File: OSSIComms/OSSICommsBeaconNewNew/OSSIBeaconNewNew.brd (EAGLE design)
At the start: 94 x 88 mm, 77 parts, among them Q1 NX-3215, U1 OPA2347, U2 MSP430F2132, U3 LM7321, U4 MAX1682, U5 MAX890L, U6 MAX4376, U7 TPS3838, U8 MCP1700_SOT23, X1 ESQ-126-38-G-D, X2 5268-03, X3 ICCON_POWERCON, X4 ICCON_POWERCON, X5 WEIDMULLER, X6 JTAG10PINMINI-H, X7 5268-03

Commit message: beacon newnew led new
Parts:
- removed JP2: (no value), OSSI:JP1
- removed LED3: (no value), SparkFun:LED-0603
- removed Q1: NX-3215, OSSI:NX-3215
- removed R33: 1k, OSSI:R0603(1608)
- removed R63, R67: 250, OSSI:R0603(1608)
- removed R71: 10k, OSSI:R0603(1608)
- removed TP1, TP2, TP3, TP4, TP5, TP6, TP7: TP, OSSI:TP-13
- removed TR2: FDV301N, OSSI:SOT23
- removed X6: JTAG10PINMINI-H, OSSI:M50-3200545
- removed X7: 5268-03, OSSI:5268-03
- added C13: 22nF, OSSI:C0603(1608)
- added C14: 1uF,0603, OSSI:C0603(1608)
- added C15: 100pF, OSSI:C0603(1608)
- added C16: 1uF 0805, OSSI:C0805(2012)
- added C19, C33: 1uF, OSSI:C0603(1608)
- added C20: (no value), OSSI:C0603(1608)
- added C21, C25: 1nF, OSSI:C0603(1608)
- added C22, C23, C24: 22pF, OSSI:C0603(1608)
- added C26, C31: 10nF, OSSI:C0603(1608)
- added C27: DNP, OSSI:C0603(1608)
- added C28: 22uF,1210, OSSI:C1210-GCM32
- added C29, C30: 10uF, LDO Tantal 16V, OSSI:C1206(3216)-A
- added C32, C34, C35, C36, C40, C42: 100nF, OSSI:C0603(1608)
- added C37, C41: TBD, OSSI:C0603(1608)
- added C38, C39: 12.5pF, OSSI:C0603(1608)
- added D1: BAT54S, OSSI:SOT23
- added F1: LFCN-160, OSSI:LFCN
- added L1, L3: 470nH, 1008 size, OSSI:L1008(2520)
- added L2: 10nH, OSSI:L0603(1608)
- added L4, L5: 68nH, OSSI:L0603(1608)
- added L6: 5~15R ferrite bead, OSSI:L0805(2012)
- added Q2: NX-3215, OSSI:NX-3215
- added R26: 4.7k, OSSI:R0603(1608)
- added R27: 47k, OSSI:R0603(1608)
- added R28: 1M, OSSI:R0603(1608)
- added TCXO1: 19.2MHz, OSSI:TCXO_M532
- added U10: NC7SZ04, OSSI:SC70-5
- added U9: MAX6369, OSSI:SOT23-8
- C1: value 1uF -> 100nF
- C10: value 100nF -> 1000pF
- C11: value 10uF, LDO Tantal 16V -> 22pF; device OSSI:C1206(3216)-A -> OSSI:C0603(1608)
- C12: value 10uF, LDO Tantal 16V -> 68pF; device OSSI:C1206(3216)-A -> OSSI:C0603(1608)
- C17: value 12.5pF -> 2.2uF, 0805; device OSSI:C0603(1608) -> OSSI:C0805(2012)
- C18: value 12.5pF -> 100pF
- C2: value 100nF -> 1uF
- C3: value 100nF -> 22uF,1210; device OSSI:C0603(1608) -> OSSI:C1210-GCM32
- C4: value 100nF -> 1uF,0805; device OSSI:C0603(1608) -> OSSI:C0805(2012)
- C6: value 10uF, LDO Tantal 16V -> 10nF; device OSSI:C1206(3216)-A -> OSSI:C0603(1608)
- C7: value 100nF -> 10nF
- C8: value 1uF 0805 -> 10nF; device OSSI:C0805(2012) -> OSSI:C0603(1608)
- C9: value 1206 Cap -> (none); device OSSI:C1206-GCM31 -> OSSI:C0603(1608)
- LED1: device led:CHIPLED_0603 -> SparkFun:LED-0603
- R1, R10: value TBD -> 100k
- R11: value 4.7k -> 23.7k
- R12, R8: value 4.7k -> 0
- R13: value 10k -> 4.7k
- R14: value 47k -> 4.7k
- R15, R17, R21: value (none) -> 100k
- R18: value 1k -> 4.7k
- R19: value (none) -> 4.7k
- R20: value (none) -> 10k
- R22: value 0.005, 2W RSENSE -> 250; device OSSI:R4527(12070) -> OSSI:R0603(1608)
- R23: value 0 -> 1k
- R24: value 1.1k -> 10k
- R25: value 2.2k -> 250
- R3: value 100k -> 6.2k
- R4: value 1k -> 100k
- R5: value 100k -> 5.1k
- R6: value 100k -> 2.4k
- R7: value 1.5k -> 3.6k
- R9: value DNP -> 100k
- TR1: value FDD8896 -> FDV301N; device OSSI:TO252 -> OSSI:SOT23
- U1: value OPA2347 -> MAX890L; device OSSI:SOT23-8DCN -> OSSI:SO8
- U2: value MSP430F2132 -> ADL5530; device OSSI:PW28 -> OSSI:LFCSP8_CP
- U3: value LM7321 -> ADF7012; device OSSI:SO8 -> OSSI:TSSOP24
- U4: value MAX1682 -> MCP1700_SOT23; device OSSI:SOT23-5DBV -> OSSI:SOT23
- U6: value MAX4376 -> TPS3838
- U7: value TPS3838 -> OPA2347; device OSSI:SOT23-5DBV -> OSSI:SOT23-8DCN
- U8: value MCP1700_SOT23 -> MSP430F2132; device OSSI:SOT23 -> OSSI:PW28
- X2: value 5268-03 -> RFCON-MCX-R/A; device OSSI:5268-03 -> OSSI:MCX-R/A
- X3: value ICCON_POWERCON -> JTAG10PINMINI-H; device OSSI:ICCON6643220-1 -> OSSI:M50-3200545
- X4: value ICCON_POWERCON -> 5268-03; device OSSI:ICCON6643220-1 -> OSSI:5268-03
- X5: value WEIDMULLER -> 5268-02; device OSSI:WEIDMULLER1760490000 -> OSSI:5628-02
- moved R4 69.1 mm to (72.4, 71.1), turned to 0 degrees
- moved U1 67.1 mm to (73.7, 59.7)
- moved C2 66.2 mm to (71.1, 64.8), turned to 180 degrees
- moved U$1 61.4 mm to (76.2, 85.1)
- moved R18 56.4 mm to (43.2, 74.3), turned to 270 degrees
- moved R2 56.4 mm to (73.7, 64.8), turned to 0 degrees
- moved X2 55.8 mm to (8.89, 19.1), turned to 90 degrees
- moved C3 54.2 mm to (25.4, 9.53)
- moved R21 51.3 mm to (8.89, 64.8), turned to 180 degrees
- moved R10 49.5 mm to (63.5, 69.8), turned to 0 degrees
- moved C9 45.7 mm to (15.2, 19.1), turned to 180 degrees
- moved C6 44.3 mm to (26.0, 15.2), turned to 180 degrees
- moved C17 43.9 mm to (56.5, 12.1), turned to 90 degrees
- moved R16 43.6 mm to (16.5, 64.8), turned to 180 degrees
- moved R19 43.2 mm to (45.7, 74.3), turned to 270 degrees
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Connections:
- removed net 3.3VLED: C10.1, C11.1, C2.1, C7.1, R10.1, R13.2, R2.2, R71.2, U1.8, U2.2, U6.3, U7.5, U8.2, X2.1, X6.4
- removed net ACLK_OUT: TP2.TP, U2.8
- removed net ADC2: U1.6, U1.7, U2.10
- removed net PWM: JP2.1, R19.2, R20.1
- removed net RESET_LED: R2.1, R8.2, U2.7, U7.4
- removed net SMCLK_OUT: TP1.TP, U2.25, X6.7
- removed net STRUT_GND: H1.B3,2
- removed net SUN: R18.2, X2.2
- new net 3.3VBEACON: C28.P$1, C30.1, C31.1, C35.1, C36.1, D1.2, L6.1, R1.2, R20.2, R24.2, R9.2, U4.2, U6.5, U7.8, U8.2, U9.4, U9.5, U9.6, U9.8, X3.4, X5.1
- new net ADC0: U7.6, U7.7, U8.8
- new net BEACON_CE: U3.14, U8.18
- new net BEACON_CWCONTROL: R26.2, R27.1, X5.2
- new net BEACON_DATA: U3.4, U8.24
- new net BEACON_MUXOUT: U3.6, U8.22
- new net BEACON_RFOUT: C24.2, C7.1, L5.2
- new net BEACON_SCLK: U3.11, U8.21
- new net BEACON_SDATA: U3.12, U8.20
- new net BEACON_SLE: U3.13, U8.19
- new net BEACON_TXCLK: U3.5, U8.23
- new net BEACON_WDT_RST: C40.1, U6.3, U9.7
- new net N$1: R23.1, U8.11
- new net N$2: U8.27, X3.3
- new net N$34: C8.2, F1.1
- new net N$35: C9.1, F1.3
- new net N$36: C23.2, L4.2, L5.1
- new net N$37: C9.2, X2.1
- new net N$38: C25.2, C27.1, R28.2, U10.2
- new net N$40: C30.2, R12.1
- new net N$666: C29.1, C34.1, U4.3, U5.6, U5.7
- new net N$69: C25.1, TCXO1.3
- new net OSC1: C27.2, U3.8
- new net OSC2: R28.1, U10.4, U3.9
- new net PA_-FAULT: R1.1, U1.8, U8.3
- new net PA_ON: R4.2, TR1.1, U8.17
- new net RESETBEACON: R14.2, R9.1, U6.4, U8.7
- new net VBEACON_PA: C1.1, C3.P$1, C4.1, C5.1, C6.1, L1.P$1, U1.6, U1.7
- new net VCCRF: C14.1, C15.1, C20.1, C26.1, C32.1, L6.2, R8.1, TCXO1.4, U10.5, U3.1
- net ADC1: now also U7.1, U7.2, U8.9; no longer U1.1, U1.2, U2.9
- net BEACON_-FAULT: now also U5.8
- net BEACON_OFF: now also C33.1, R10.2, U5.3
- net BEACON_SCL: now also R24.1, R25.1
- net BEACON_SDA: now also R20.1, R22.1
- net BUS_CS: now also R15.1
- net GND: now also C11.2, C12.1, C14.2, C15.2, C16.1, C17.1, C19.2, C20.2, C22.1, C23.1, C24.1, C26.2, C28.P$2, C29.2, C3.P$2, C31.2, C32.2, C33.2, C34.2, C35.2, C36.2, C37.2, C38.2, C39.2, C40.2, C41.2, C42.2, C6.2, D1.1, F1.2, F1.4, R10.1, R11.1, R12.2, R13.2, R16.2, R27.2, R4.1, R7.1, TCXO1.1, TCXO1.2, TR1.2, U10.3, U2.1, U2.3, U2.5, U2.6, U2.8, U3.19, U3.22, U3.7, U6.1, U7.4, U8.4, U9.2, X2.2, X2.4, X2.5, X3.9; no longer C10.2, C12.2, C17.2, C3.2, C7.2, C8.2, C9.P$2, LED3.C, R1.1, R14.1, R17.2, R20.2, R23.2, R24.2, R25.1, R9.2, TP3.TP, TR2.2, U3.4, U7.1, U7.2, U8.1, X4.10, X4.2, X4.3, X4.4, X4.5, X4.6, X4.7, X4.8, X4.9, X5.2, X6.9, X7.1
- net LED_-FAULT: no longer U5.8
- net LED_OFF: no longer C1.1, R3.2, U5.3
- net LED_SCL: no longer R67.1, R71.1
- net LED_SDA: no longer R13.1, R63.1
- net N$10: now also R25.2, U8.13; no longer R1.2, U5.5
- net N$11: now also R18.2, U8.16; no longer R4.2, R5.2, R6.1
- net N$12: now also U8.10, U9.1; no longer R22.P$2, R7.1, TP6.TP, U6.5, X3.1, X3.10, X3.2, X3.3, X3.4, X3.5, X3.6, X3.7, X3.8, X3.9
- net N$13: now also C42.1, D1.3, R26.1, U8.14; no longer C9.P$1, U3.7, U4.2
- net N$14: now also L2.1, U3.16; no longer R16.1, R25.2, U3.6
- net N$15: now also L2.2, U3.15; no longer U2.27, X6.3
- net N$16: now also C13.1, C16.2, U3.24; no longer R22.P$1, TP7.TP, TR1.S, U6.4
- net N$17: now also C13.2, U3.17; no longer C11.2, R23.1
- net N$18: now also R7.2, U3.23; no longer R24.1, U3.2
- net N$19: now also C2.1, R2.1, TR1.3, U1.3; no longer C17.1, Q1.2, U2.5
- net N$20: now also C10.1, R6.1; no longer C18.1, Q1.1, U2.6
- net N$21: now also R3.2, U1.5; no longer JP1.2, LED3.A, R33.2
- net N$22: now also C41.1, R17.2, R21.1, U7.5; no longer R63.2, U2.12
- net N$23: now also C21.2, L3.P$2, U3.20; no longer R67.2, U2.13
- net N$24: now also C11.1, R5.1, U3.18; no longer R15.1, U6.1
- net N$25: now also C17.2, U3.2; no longer R33.1, U2.14
- net N$26: now also C10.2, C12.2, R5.2, U3.3; no longer C6.2, U4.3
- net N$27: now also C18.1, C19.1, L3.P$1, R8.2, U3.21; no longer C6.1, U4.5
- net N$28: now also C7.2, U2.2; no longer R12.2, U2.16
- net N$29: now also C21.1, C22.2, L4.1; no longer LED1.A, R7.2
- net N$3: now also U8.26, X3.5; no longer U2.28, X6.1
- net N$30: now also C8.1, L1.P$2, U2.7; no longer R15.2, R17.1, TR2.1
- net N$31: now also R14.1, X3.10; no longer U2.26, X6.5
- net N$32: now also R11.2, U5.5; no longer R8.1, X6.10
- net N$33: now also C37.1, R15.2, R16.1, U7.3; no longer JP2.2, U2.18
- net N$39: now also R19.2, U8.15; no longer R11.2, U2.15
- net N$4: now also U8.25, X3.7; no longer R10.2, U2.3
- net N$5: now also C38.1, Q2.2, U8.5; no longer C12.1, C3.1, U5.6, U5.7, U8.3
- net N$6: now also C39.1, Q2.1, U8.6; no longer R16.2, R9.1, TP5.TP, TR1.G, TR2.3
- net N$7: now also JP1.2, LED1.A, R23.2; no longer C4.1, R4.1, U1.3
- net N$8: now also U8.28, X3.1; no longer C5.1, R18.1, U1.5
- net N$9: now also R22.2, U8.12; no longer R19.1, R21.1, U3.3
- net RXD: now also R18.1, X4.3; no longer R12.1, X7.3
- net TEST: now also R13.1, U8.1, X3.8; no longer R14.2, U2.1, X6.8
- net TXD: now also R19.1, X4.2; no longer R11.1, X7.2
- net VBUS: now also R17.1, R2.2, U1.1, U1.2
- net VSUPERCAP: now also X1.13; no longer C8.1, R5.1, TP4.TP, TR1.D, U4.4, X5.1
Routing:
- net 3.3VLED: track 226.5 -> 0.00 mm, vias 2 -> 0
- net VSUPERCAP: track 89.2 -> 0.00 mm, vias 23 -> 0
- net LED_SCL: track 85.9 -> 0.00 mm, vias 2 -> 0
- net LED_SDA: track 82.0 -> 0.00 mm, vias 2 -> 0
- net BEACON_DATA: track 0.00 -> 65.5 mm
- net BEACON_TXCLK: track 0.00 -> 63.3 mm
- net BEACON_MUXOUT: track 0.00 -> 61.1 mm
- net SUN: track 52.8 -> 0.00 mm
- net BEACON_SLE: track 0.00 -> 49.5 mm
- net BEACON_CE: track 0.00 -> 49.4 mm
- net N$3: track 46.7 -> 0.00 mm, vias 2 -> 0
- net RESET_LED: track 46.2 -> 0.00 mm, vias 2 -> 0
- net SMCLK_OUT: track 45.4 -> 0.00 mm, vias 2 -> 0
- net N$31: track 43.4 -> 0.00 mm, vias 2 -> 0
- net N$15: track 45.0 -> 4.12 mm, vias 2 -> 0
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- removed copper zone on layer 1, net GND
- removed copper zone on layer 16, net GND
- removed copper zone on layer 16, net N$1
- removed copper zone on layer 1, net N$12
- removed copper zone on layer 1, net N$16
- removed copper zone on layer 16, net N$2
- removed copper zone on layer 16, net N$56
- removed copper zone on layer 1, net N$6
- removed copper zone on layer 1, net STRUT_GND
- removed copper zone on layer 1, net VBUS
- removed copper zone on layer 1, net VSOLAR
- removed copper zone on layer 1, net VSUPERCAP
- removed copper zone on layer 16, net VSUPERCAP
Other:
- board size 94 x 88 mm -> 92 x 92 mm
- board text removed: "ACLK"
- board text removed: "GND"
- board text removed: "LED+"
- board text removed: "PWM"
- board text removed: "RXD"
- board text removed: "SMCLK"
- board text removed: "SUN"
- board text removed: "TXD"
- board text removed: "VLED"
- board text removed: "VSUPERCAP"

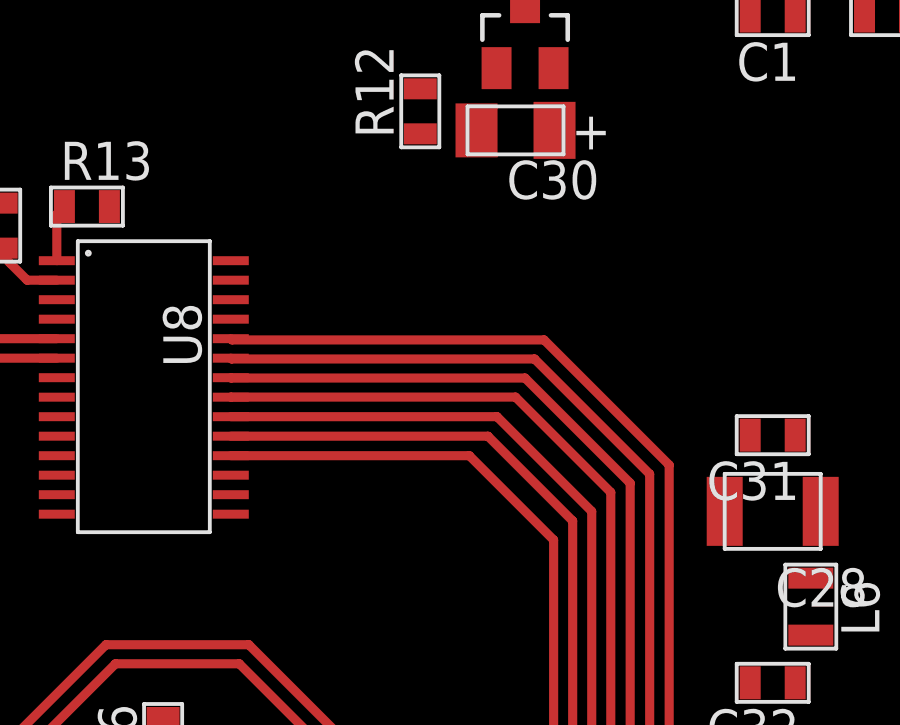
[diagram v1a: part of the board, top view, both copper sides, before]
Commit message: series resistor added
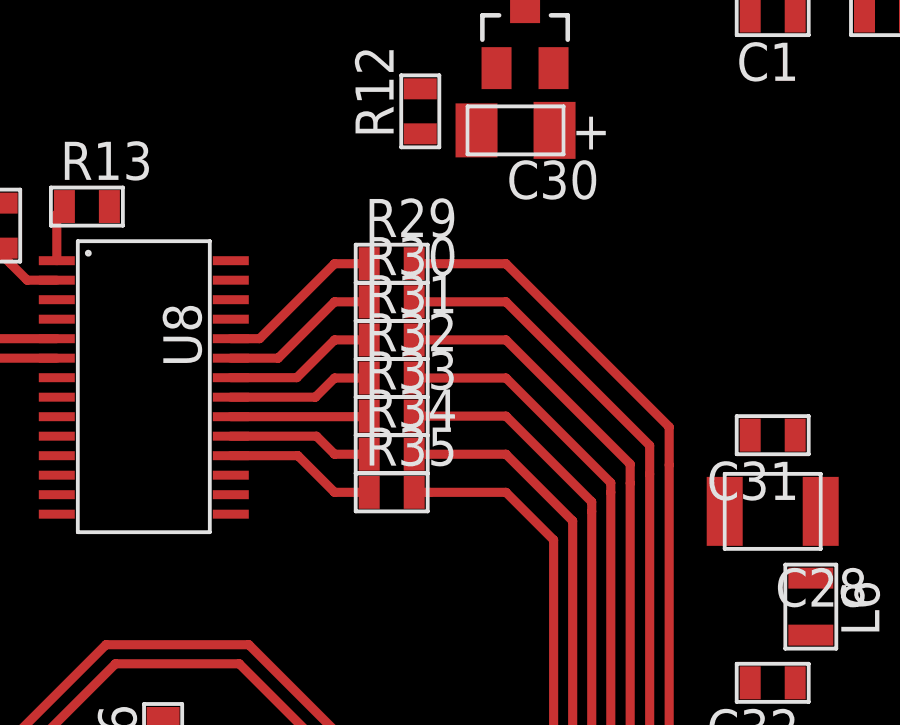
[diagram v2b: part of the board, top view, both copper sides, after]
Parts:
- added R29, R30, R31, R32, R33, R34, R35: 4.7k, OSSI:R0603(1608)
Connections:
- new net N$41: R29.1, U8.24
- new net N$42: R30.1, U8.23
- new net N$43: R31.1, U8.22
- new net N$44: R32.1, U8.21
- new net N$45: R33.1, U8.20
- new net N$46: R34.1, U8.19
- new net N$47: R35.1, U8.18
- net BEACON_CE: now also R35.2; no longer U8.18
- net BEACON_DATA: now also R29.2; no longer U8.24
- net BEACON_MUXOUT: now also R31.2; no longer U8.22
- net BEACON_SCLK: now also R32.2; no longer U8.21
- net BEACON_SDATA: now also R33.2; no longer U8.20
- net BEACON_SLE: now also R34.2; no longer U8.19
- net BEACON_TXCLK: now also R30.2; no longer U8.23
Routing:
- net BEACON_CE: track 49.4 -> 42.8 mm
- net BEACON_SLE: track 49.5 -> 43.2 mm
- net BEACON_SDATA: track 37.0 -> 31.1 mm
- net BEACON_SCLK: track 39.8 -> 34.1 mm
- net N$41: track 0.00 -> 5.65 mm
- net N$42: track 0.00 -> 5.39 mm
- net BEACON_MUXOUT: track 61.1 -> 55.9 mm
- net N$43: track 0.00 -> 5.13 mm
- net N$47: track 0.00 -> 5.12 mm
- net N$44: track 0.00 -> 4.88 mm
- net N$46: track 0.00 -> 4.86 mm
- net BEACON_TXCLK: track 63.3 -> 58.5 mm
- net N$45: track 0.00 -> 4.62 mm
- net BEACON_DATA: track 65.5 -> 61.1 mm

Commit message: beacon almost done
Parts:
- moved R4 35.6 mm to (56.2, 39.4), turned to 90 degrees
- moved TR1 32.2 mm to (58.7, 39.4), turned to 270 degrees
- moved C37 29.3 mm to (22.9, 37.5)
- moved R1 28.0 mm to (48.3, 55.2), turned to 180 degrees
- moved R15 26.8 mm to (25.4, 38.7)
- moved R16 26.8 mm to (22.9, 38.7)
- moved C41 23.1 mm to (22.9, 47.6)
- moved R17 23.1 mm to (25.4, 46.4)
- moved R21 23.1 mm to (22.9, 46.4)
- moved U7 20.4 mm to (22.9, 42.5), turned to 0 degrees
- moved C35 17.1 mm to (20.3, 42.5), turned to 270 degrees
- moved R23 12.6 mm to (30.8, 54.9), turned to 90 degrees
- moved C40 10.6 mm to (29.5, 48.3), turned to 90 degrees
- moved R2 10.2 mm to (73.7, 74.9)
- moved C1 9.52 mm to (72.4, 63.5)
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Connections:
- new net STRUT_GND: H1.B3,2
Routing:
- net 3.3VBEACON: track 2.42 -> 200.3 mm, vias 0 -> 8
- net VBUS: track 0.00 -> 122.6 mm, vias 0 -> 1
- net VBEACON_PA: track 7.44 -> 120.3 mm
- net N$2: track 0.00 -> 100.0 mm, vias 0 -> 1
- net VCCRF: track 19.0 -> 87.1 mm, vias 0 -> 4
- net BUS_CS: track 0.00 -> 67.8 mm, vias 0 -> 1
- net RESETBEACON: track 0.00 -> 63.2 mm, vias 0 -> 4
- net N$19: track 0.00 -> 53.7 mm, vias 0 -> 4
- net GND: track 4.46 -> 54.5 mm, vias 0 -> 207
- net PA_-FAULT: track 0.00 -> 49.4 mm, vias 0 -> 2
- net BEACON_SDA: track 0.00 -> 49.0 mm, vias 0 -> 1
- net BEACON_SCL: track 0.00 -> 46.8 mm, vias 0 -> 1
- net TEST: track 1.91 -> 45.7 mm, vias 0 -> 1
- net N$13: track 0.00 -> 42.8 mm, vias 0 -> 2
- net BEACON_OFF: track 0.00 -> 42.5 mm, vias 0 -> 2
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- added copper zone on layer 1, net GND
- added copper zone on layer 16, net GND
- added copper zone on layer 1, net N$23
- added copper zone on layer 16, net N$48
- added copper zone on layer 16, net N$49
- added copper zone on layer 16, net N$50
- added copper zone on layer 16, net N$51
- added copper zone on layer 1, net STRUT_GND
- added copper zone on layer 1, net VBUS
- added copper zone on layer 1, net VSOLAR

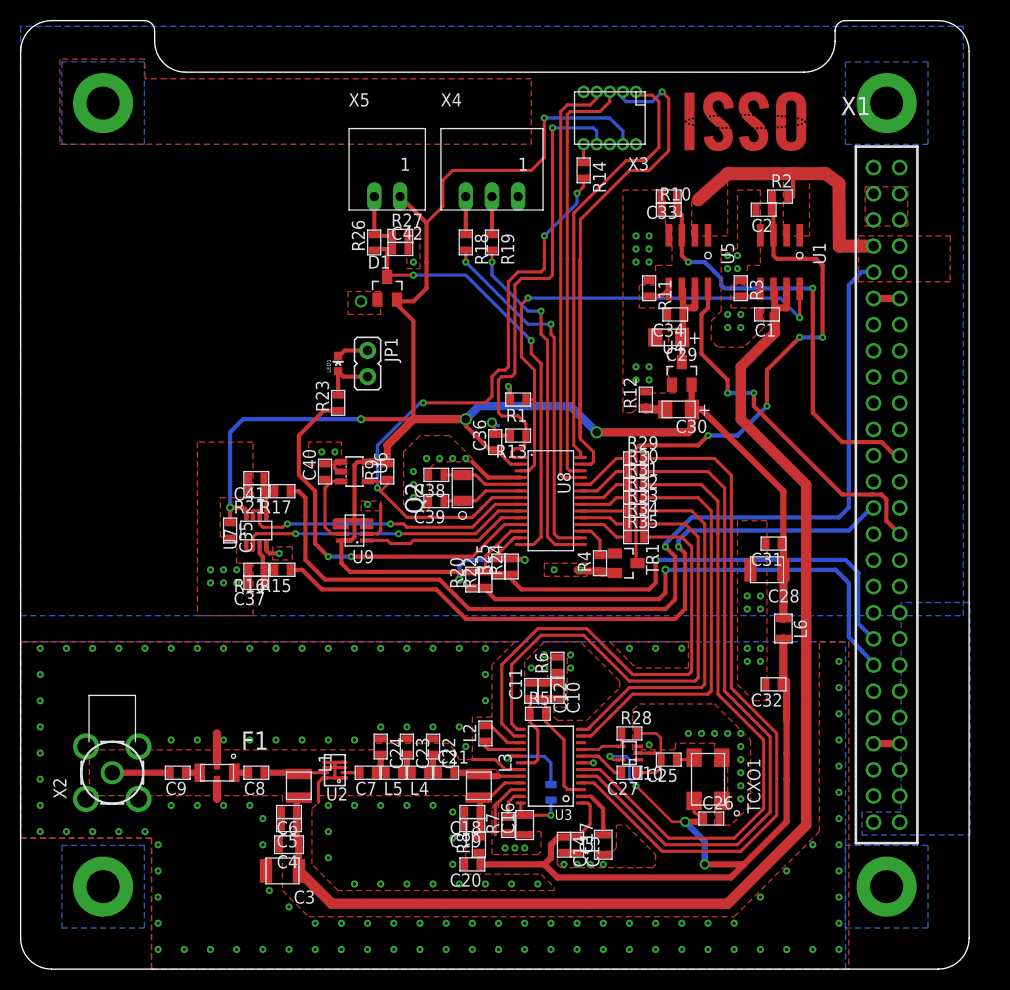
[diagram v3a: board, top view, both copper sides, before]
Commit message: gerber files are created / led current setting fixed to 9.7A
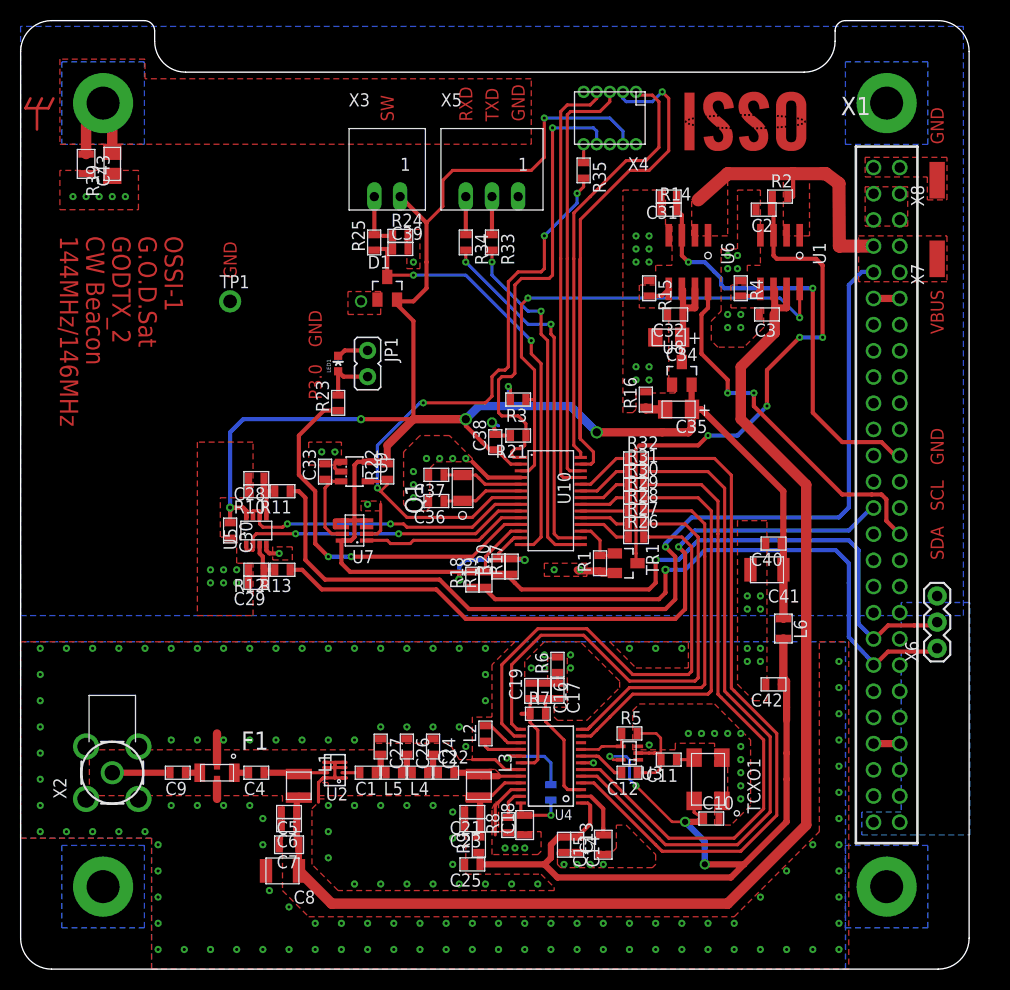
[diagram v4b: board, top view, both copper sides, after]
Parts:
- added C43: (no value), OSSI:C0805(2012)
- added R39: 511, OSSI:WSL1206
- added TP1: TP, OSSI:TP-13
- added X6: (no value), OSSI:1X03
- added X7, X8: P-PAD-S, OSSI:P-PAD-S
- C1, C40, C5: value 100nF -> 10nF
- C10: value 1000pF -> 10nF
- C11, C22: value 22pF -> 1nF
- C12: value 68pF -> DNP
- C13: value 22nF -> 2.2uF, 0805; device OSSI:C0603(1608) -> OSSI:C0805(2012)
- C14: value 1uF,0603 -> 100pF
- C15: value 100pF -> 1uF,0603
- C16: value 1uF 0805 -> 68pF; device OSSI:C0805(2012) -> OSSI:C0603(1608)
- C17: value 2.2uF, 0805 -> 1000pF; device OSSI:C0805(2012) -> OSSI:C0603(1608)
- C18: value 100pF -> 1uF 0805; device OSSI:C0603(1608) -> OSSI:C0805(2012)
- C19: value 1uF -> 22pF
- C20: value (none) -> 22nF
- C21: value 1nF -> 100pF
- C23: value 22pF -> 1uF
- C25: value 1nF -> (none)
- C26: value 10nF -> 22pF
- C27: value DNP -> 22pF
- C28: value 22uF,1210 -> TBD; device OSSI:C1210-GCM32 -> OSSI:C0603(1608)
- C29: value 10uF, LDO Tantal 16V -> TBD; device OSSI:C1206(3216)-A -> OSSI:C0603(1608)
- C3: value 22uF,1210 -> 100nF; device OSSI:C1210-GCM32 -> OSSI:C0603(1608)
- C30: value 10uF, LDO Tantal 16V -> 100nF; device OSSI:C1206(3216)-A -> OSSI:C0603(1608)
- C31: value 10nF -> 1uF
- C33: value 1uF -> 100nF
- C34, C35: value 100nF -> 10uF, LDO Tantal 16V; device OSSI:C0603(1608) -> OSSI:C1206(3216)-A
- C36: value 100nF -> 12.5pF
- C37: value TBD -> 12.5pF
- C38, C39: value 12.5pF -> 100nF
- C4: value 1uF,0805 -> 10nF; device OSSI:C0805(2012) -> OSSI:C0603(1608)
- C41: value TBD -> 22uF,1210; device OSSI:C0603(1608) -> OSSI:C1210-GCM32
- C6: value 10nF -> 100nF
- C7: value 10nF -> 1uF,0805; device OSSI:C0603(1608) -> OSSI:C0805(2012)
- C8: value 10nF -> 22uF,1210; device OSSI:C0603(1608) -> OSSI:C1210-GCM32
- R11: value 23.7k -> 100k
- R12: value 0 -> 100k
- R13, R14: value 4.7k -> 100k
- R15: value 100k -> 23.7k
- R16, R9: value 100k -> 0
- R17: value 100k -> 10k
- R18: value 4.7k -> 10k
- R19: value 4.7k -> 250
- R20: value 10k -> 250
- R21: value 100k -> 4.7k
- R22: value 250 -> 100k
- R24: value 10k -> 47k
- R25: value 250 -> 4.7k
- R27: value 47k -> 4.7k
- R28: value 1M -> 4.7k
- R3: value 6.2k -> 100k
- R4: value 100k -> 6.2k
- R5: value 5.1k -> 1M
- R7: value 3.6k -> 5.1k
- R8: value 0 -> 3.6k
- U10: value NC7SZ04 -> MSP430F2132; device OSSI:SC70-5 -> OSSI:PW28
- U3: value ADF7012 -> NC7SZ04; device OSSI:TSSOP24 -> OSSI:SC70-5
- U4: value MCP1700_SOT23 -> ADF7012; device OSSI:SOT23 -> OSSI:TSSOP24
- U5: value MAX890L -> OPA2347; device OSSI:SO8 -> OSSI:SOT23-8DCN
- U6: value TPS3838 -> MAX890L; device OSSI:SOT23-5DBV -> OSSI:SO8
- U7: value OPA2347 -> MAX6369; device OSSI:SOT23-8DCN -> OSSI:SOT23-8
- U8: value MSP430F2132 -> MCP1700_SOT23; device OSSI:PW28 -> OSSI:SOT23
- U9: value MAX6369 -> TPS3838; device OSSI:SOT23-8 -> OSSI:SOT23-5DBV
- X3: value JTAG10PINMINI-H -> 5268-02; device OSSI:M50-3200545 -> OSSI:5628-02
- X4: value 5268-03 -> JTAG10PINMINI-H; device OSSI:5268-03 -> OSSI:M50-3200545
- X5: value 5268-02 -> 5268-03; device OSSI:5628-02 -> OSSI:5268-03
- moved H1 76.0 mm to (8.00, 8.00)
- moved H2 76.0 mm to (84.0, 8.00)
- moved H3 76.0 mm to (84.0, 84.0)
- moved H4 76.0 mm to (8.00, 84.0)
- moved C3 71.6 mm to (72.4, 63.5)
- moved C1 59.0 mm to (33.7, 19.1)
- moved C42 55.6 mm to (73.0, 27.6), turned to 180 degrees
- moved C28 50.3 mm to (22.9, 47.6)
- moved C41 50.3 mm to (72.4, 38.7)
- moved U5 49.3 mm to (22.9, 42.5), turned to 0 degrees
- moved R10 48.4 mm to (22.9, 46.4), turned to 180 degrees
- moved C29 46.6 mm to (22.9, 37.5)
- moved C30 45.1 mm to (20.3, 42.5), turned to 270 degrees
- moved C35 45.1 mm to (63.8, 54.3), turned to 180 degrees
- moved R15 44.8 mm to (61.0, 66.0), turned to 270 degrees
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- renumbered Q2 to Q1
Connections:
- net 3.3VBEACON: now also C38.1, C40.1, C41.P$1, R17.2, R18.2, R22.2, R3.2, U10.2, U5.8, U7.4, U7.5, U7.6, X3.1, X4.4; no longer C28.P$1, C31.1, C36.1, R1.2, R20.2, R24.2, R9.2, U4.2, U6.5, U9.4, U9.6, U9.8, X3.4, X5.1
- net ADC0: now also U10.8, U5.6, U5.7; no longer U7.6, U7.7, U8.8
- net ADC1: now also U10.9, U5.1, U5.2; no longer U7.1, U7.2, U8.9
- net BEACON_-FAULT: now also U6.8; no longer U5.8
- net BEACON_CE: now also R26.2, U4.14; no longer R35.2, U3.14
- net BEACON_CWCONTROL: now also R24.1, R25.2, X3.2; no longer R26.2, R27.1, X5.2
- net BEACON_DATA: now also R32.2, U4.4; no longer R29.2, U3.4
- net BEACON_MUXOUT: now also R30.2, U4.6; no longer R31.2, U3.6
- net BEACON_OFF: now also C31.1, R14.2, U6.3; no longer C33.1, R10.2, U5.3
- net BEACON_RFOUT: now also C1.1, C27.2; no longer C24.2, C7.1
- net BEACON_SCL: now also R17.1, R20.1, X6.2; no longer R24.1, R25.1
- net BEACON_SCLK: now also R29.2, U4.11; no longer R32.2, U3.11
- net BEACON_SDA: now also R18.1, R19.1, X6.1; no longer R20.1, R22.1
- net BEACON_SDATA: now also R28.2, U4.12; no longer R33.2, U3.12
- net BEACON_SLE: now also R27.2, U4.13; no longer R34.2, U3.13
- net BEACON_TXCLK: now also R31.2, U4.5; no longer R30.2, U3.5
- net BEACON_WDT_RST: now also C33.1, U7.7, U9.3; no longer C40.1, U6.3, U9.7
- net BUS_CS: now also R13.1; no longer R15.1
- net GND: now also C10.2, C13.1, C18.1, C21.2, C23.2, C25.2, C26.1, C27.1, C28.2, C3.2, C30.2, C41.P$2, C43.2, C7.2, C8.P$2, R1.1, R10.2, R14.1, R15.1, R24.2, R39.P$1, R8.1, TP1.TP, U10.4, U3.3, U4.19, U4.22, U4.7, U6.4, U7.2, U8.1, U9.1, X4.9, X5.1, X6.3, X8.1; no longer C1.2, C11.2, C12.1, C17.1, C18.2, C20.2, C22.1, C23.1, C26.2, C28.P$2, C3.P$2, C35.2, C4.2, C41.2, R10.1, R11.1, R13.2, R27.2, R3.1, R7.1, U10.3, U3.19, U3.22, U3.7, U4.1, U6.1, U6.2, U7.4, U8.4, X3.9, X4.1
- net N$1: now also U10.11; no longer U8.11
- net N$10: now also R20.2, U10.13; no longer R25.2, U8.13
- net N$11: now also R34.2, U10.16; no longer R18.2, U8.16
- net N$12: now also U10.10, U7.1; no longer U8.10, U9.1
- net N$13: now also C39.1, R25.1, U10.14; no longer C42.1, R26.1, U8.14
- net N$14: now also U4.16; no longer U3.16
- net N$15: now also U4.15; no longer U3.15
- net N$16: now also C18.2, C20.1, U4.24; no longer C13.1, C16.2, U3.24
- net N$17: now also C20.2, U4.17; no longer C13.2, U3.17
- net N$18: now also R8.2, U4.23; no longer R7.2, U3.23
- net N$2: now also U10.27, X4.3; no longer U8.27, X3.3
- net N$20: now also C17.1; no longer C10.1
- net N$21: now also R4.2; no longer R3.2
- net N$22: now also C28.1, R10.1, R11.2, U5.5; no longer C41.1, R17.2, R21.1, U7.5
- net N$23: now also C22.2, U4.20; no longer C21.2, U3.20
- net N$24: now also C19.1, R7.1, U4.18; no longer C11.1, R5.1, U3.18
- net N$25: now also C13.2, U4.2; no longer C17.2, U3.2
- net N$26: now also C16.2, C17.2, R7.2, U4.3; no longer C10.2, C12.2, R5.2, U3.3
- net N$27: now also C21.1, C23.1, R9.2, U4.21; no longer C18.1, C19.1, R8.2, U3.21
- net N$28: now also C1.2; no longer C7.2
- net N$29: now also C22.1, C24.2; no longer C21.1, C22.2
- net N$3: now also U10.26, X4.5; no longer U8.26, X3.5
- net N$30: now also C4.1; no longer C8.1
- net N$31: now also R35.1, X4.10; no longer R14.1, X3.10
- net N$32: now also R15.2, U6.5; no longer R11.2, U5.5
- net N$33: now also C29.1, R12.1, R13.2, U5.3; no longer C37.1, R15.2, R16.1, U7.3
- net N$34: now also C4.2; no longer C8.2
- net N$36: now also C26.2; no longer C23.2
- net N$38: now also C11.2, C12.1, R5.2, U3.2; no longer C25.2, C27.1, R28.2, U10.2
- net N$39: now also R33.2, U10.15; no longer R19.2, U8.15
- net N$4: now also U10.25, X4.7; no longer U8.25, X3.7
- net N$40: now also C35.2, R16.1; no longer C30.2, R12.1
- net N$41: now also R32.1, U10.24; no longer R29.1, U8.24
- net N$42: now also R31.1, U10.23; no longer R30.1, U8.23
- net N$43: now also R30.1, U10.22; no longer R31.1, U8.22
- net N$44: now also R29.1, U10.21; no longer R32.1, U8.21
- net N$45: now also R28.1, U10.20; no longer R33.1, U8.20
- net N$46: now also R27.1, U10.19; no longer R34.1, U8.19
- net N$47: now also R26.1, U10.18; no longer R35.1, U8.18
- net N$5: now also C37.1, U10.5; no longer C38.1, U8.5
- net N$6: now also C36.1, U10.6; no longer C39.1, U8.6
- net N$666: now also C32.1, U6.6, U6.7, U8.3; no longer C29.1, U4.3, U5.6, U5.7
- net N$69: now also C11.1; no longer C25.1
- net N$8: now also U10.28, X4.1; no longer U8.28, X3.1
- net N$9: now also R19.2, U10.12; no longer R22.2, U8.12
- net OSC1: now also C12.2, U4.8; no longer C27.2, U3.8
- net OSC2: now also R5.1, U3.4, U4.9; no longer R28.1, U10.4, U3.9
- net PA_-FAULT: now also R3.1, U10.3; no longer R1.1, U8.3
- net PA_ON: now also R1.2, U10.17; no longer R4.2, U8.17
- net RESETBEACON: now also R22.1, R35.2, U10.7, U9.4; no longer R14.2, R9.1, U6.4, U8.7
- net RXD: now also R34.1, X5.3; no longer R18.1, X4.3
- net STRUT_GND: now also C43.1, H4.B3,2, R39.P$2; no longer H1.B3,2
- net TEST: now also R21.1, U10.1, X4.8; no longer R13.1, U8.1, X3.8
- net TXD: now also R33.1, X5.2; no longer R19.1, X4.2
- net VBEACON_PA: now also C3.1, C7.1, C8.P$1; no longer C1.1, C3.P$1, C4.1
- net VBUS: now also R11.1, U6.1, U6.2, X7.1; no longer R17.1, U5.1, U5.2
- net VCCRF: now also C10.1, C25.1, C42.1, R9.1, U3.5, U4.1; no longer C20.1, C26.1, C32.1, R8.1, U10.5, U3.1
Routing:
- net BEACON_SCL: track 46.8 -> 56.5 mm
- net BEACON_SDA: track 49.0 -> 58.6 mm
- net STRUT_GND: track 0.00 -> 5.82 mm
- net N$59: track 0.00 -> 5.42 mm
- net N$58: track 0.00 -> 1.91 mm
- net N$24: track 8.93 -> 9.76 mm
- net GND: vias 207 -> 212
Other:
- board text added: "144MHz/146MHz"
- board text added: "CW Beacon"
- board text added: "G.O.D.Sat"
- board text added: "GND"
- board text added: "GODTX_2"
- board text added: "OSSI-1"
- board text added: "P3.0"
- board text added: "RXD"
- board text added: "SCL"
- board text added: "SDA"
- board text added: "SW"
- board text added: "TXD"
- board text added: "VBUS"
